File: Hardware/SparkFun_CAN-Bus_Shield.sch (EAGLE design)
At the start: 48 parts, among them Q1 16MHz, U1 USD-SOCKETNEW, U2 ARDUINO_R3_SHIELD, U3 JST_VERTICAL, U4 MCP2515, U5 MCP2551, U6 HEX_CONVERTER, X1 DB9 Plug

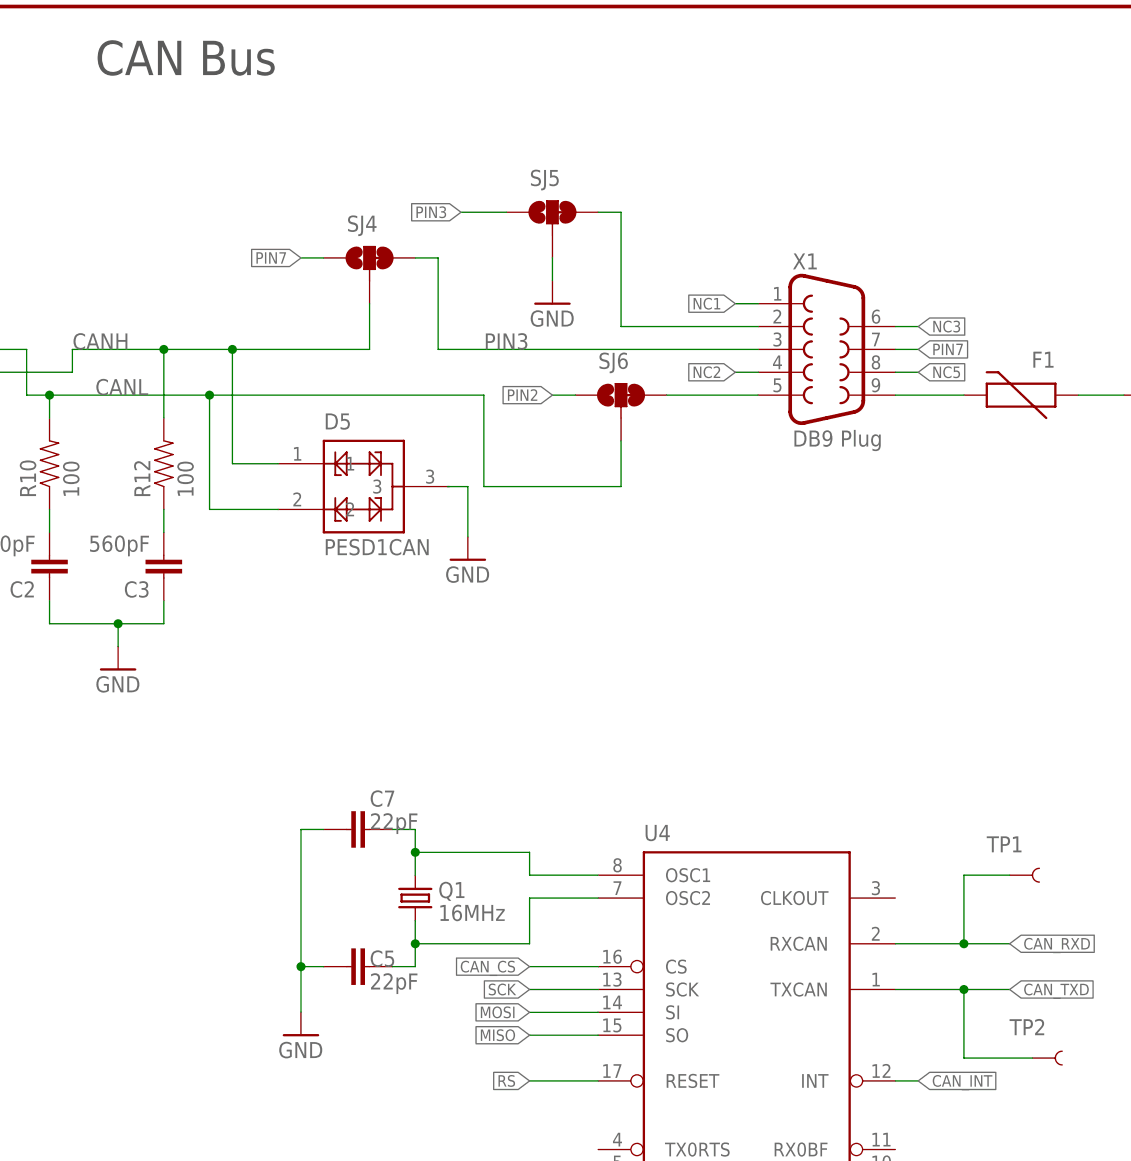
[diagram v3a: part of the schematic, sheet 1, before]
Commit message: Adding in feedback from Sukkin, and engineering review/QC checklist
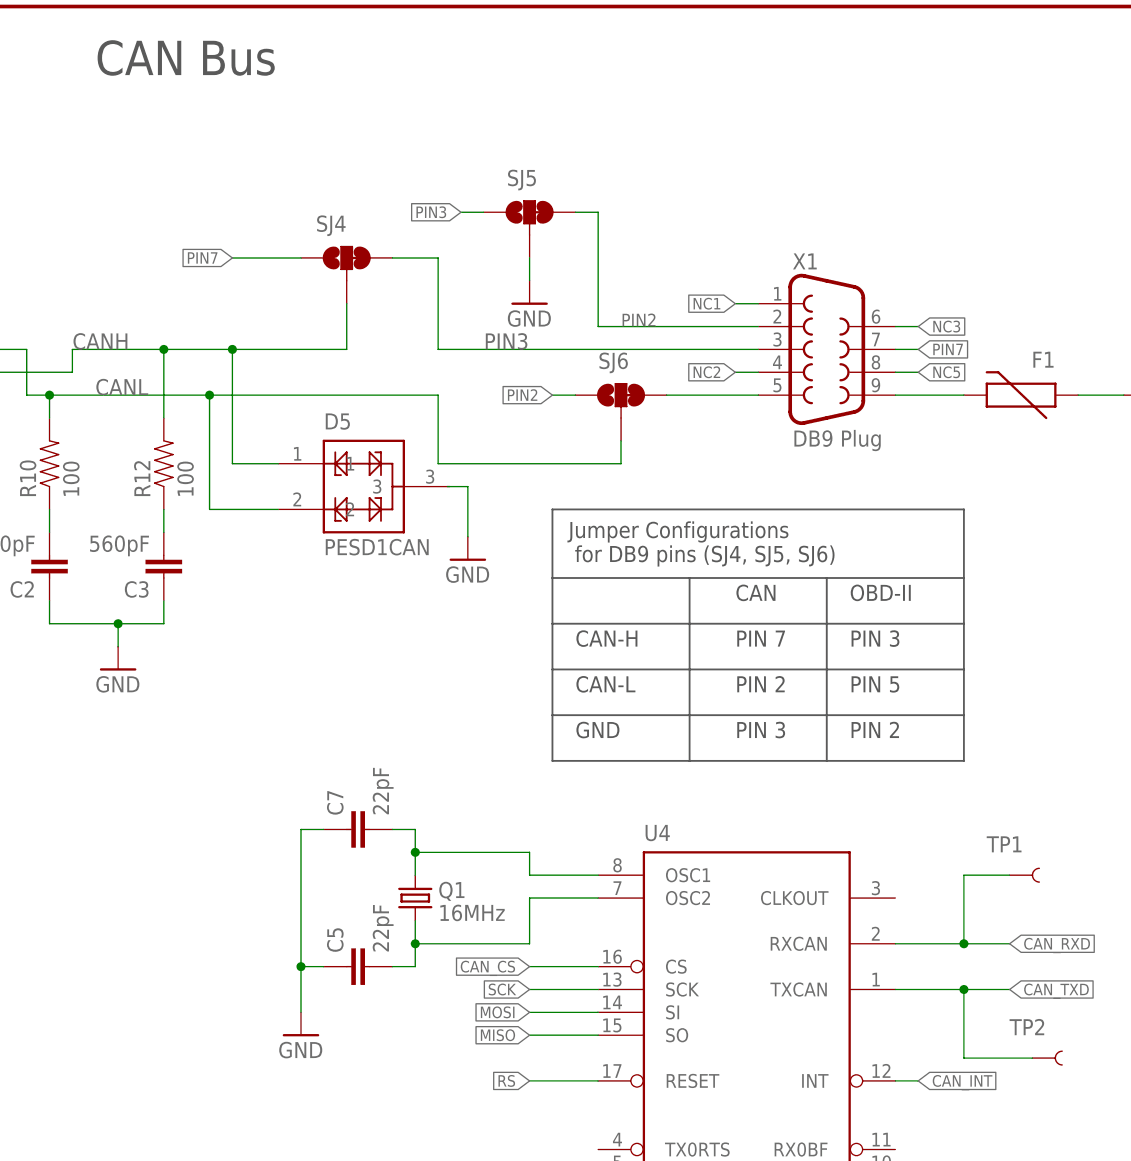
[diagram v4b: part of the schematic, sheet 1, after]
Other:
- note added: "CAN"
- note added: "CAN-H"
- note added: "CAN-L"
- note added: "GND"
- note added: "Jumper Configurations for DB9 pins (SJ4, SJ5, SJ6)"
- note added: "OBD-II"
- note added: "PIN 2"
- note added: "PIN 3"
- note added: "PIN 5"
- note added: "PIN 7"
- moved on the sheet: SJ4, SJ5
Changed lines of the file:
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@@
 <setting verticaltext="up"/>
 </settings>
-<grid distance="0.01" unitdist="inch" unit="inch" style="lines" multiple="1" display="no" altdistance="0.01" altunitdist="inch" altunit="inch"/>
+<grid distance="0.1" unitdist="inch" unit="inch" style="lines" multiple="1" display="no" altdistance="0.01" altunitdist="inch" altunit="inch"/>
 <layers>
 <layer number="1" name="Top" color="4" fill="1" visible="no" active="no"/>
@@
 <wire x1="91.44" y1="185.42" x2="93.98" y2="185.42" width="0.2032" layer="97" style="shortdash"/>
 <text x="99.06" y="177.8" size="3.81" layer="97">CAN Bus</text>
+<wire x1="149.86" y1="121.92" x2="165.1" y2="121.92" width="0.2032" layer="97"/>
+<wire x1="165.1" y1="121.92" x2="180.34" y2="121.92" width="0.2032" layer="97"/>
+<wire x1="180.34" y1="121.92" x2="195.58" y2="121.92" width="0.2032" layer="97"/>
+<wire x1="195.58" y1="121.92" x2="195.58" y2="116.84" width="0.2032" layer="97"/>
+<wire x1="195.58" y1="116.84" x2="195.58" y2="111.76" width="0.2032" layer="97"/>
+<wire x1="195.58" y1="111.76" x2="195.58" y2="106.68" width="0.2032" layer="97"/>
+<wire x1="195.58" y1="106.68" x2="195.58" y2="101.6" width="0.2032" layer="97"/>
+<wire x1="195.58" y1="101.6" x2="180.34" y2="101.6" width="0.2032" layer="97"/>
+<wire x1="180.34" y1="101.6" x2="165.1" y2="101.6" width="0.2032" layer="97"/>
+<wire x1="165.1" y1="101.6" x2="149.86" y2="101.6" width="0.2032" layer="97"/>
+<wire x1="149.86" y1="101.6" x2="149.86" y2="106.68" width="0.2032" layer="97"/>
+<wire x1="149.86" y1="106.68" x2="149.86" y2="111.76" width="0.2032" layer="97"/>
+<wire x1="149.86" y1="111.76" x2="149.86" y2="116.84" width="0.2032" layer="97"/>
+<wire x1="149.86" y1="116.84" x2="149.86" y2="121.92" width="0.2032" layer="97"/>
+<wire x1="149.86" y1="116.84" x2="195.58" y2="116.84" width="0.2032" layer="97"/>
+<wire x1="149.86" y1="111.76" x2="195.58" y2="111.76" width="0.2032" layer="97"/>
+<wire x1="149.86" y1="106.68" x2="195.58" y2="106.68" width="0.2032" layer="97"/>
+<wire x1="165.1" y1="121.92" x2="165.1" y2="101.6" width="0.2032" layer="97"/>
+<wire x1="180.34" y1="121.92" x2="180.34" y2="101.6" width="0.2032" layer="97"/>
+<text x="170.18" y="119.38" size="1.778" layer="97">CAN</text>
+<text x="182.88" y="119.38" size="1.778" layer="97">OBD-II</text>
+<text x="152.4" y="114.3" size="1.778" layer="97">CAN-H</text>
+<text x="152.4" y="109.22" size="1.778" layer="97">CAN-L</text>
+<text x="152.4" y="104.14" size="1.778" layer="97">GND</text>
+<text x="182.88" y="109.22" size="1.778" layer="97">PIN 5</text>
+<text x="182.88" y="104.14" size="1.778" layer="97">PIN 2</text>
+<text x="182.88" y="114.3" size="1.778" layer="97">PIN 3</text>
+<text x="170.18" y="109.22" size="1.778" layer="97">PIN 2</text>
+<text x="170.18" y="104.14" size="1.778" layer="97">PIN 3</text>
+<text x="170.18" y="114.3" size="1.778" layer="97">PIN 7</text>
+<wire x1="149.86" y1="121.92" x2="149.86" y2="129.54" width="0.2032" layer="97"/>
+<wire x1="149.86" y1="129.54" x2="195.58" y2="129.54" width="0.2032" layer="97"/>
+<wire x1="195.58" y1="129.54" x2="195.58" y2="121.92" width="0.2032" layer="97"/>
+<text x="151.638" y="123.698" size="1.778" layer="97">Jumper Configurations
+ for DB9 pins (SJ4, SJ5, SJ6)</text>
 </plain>
 <instances>
@@
 <attribute name="VALUE" x="137.16" y="83.82" size="1.778" layer="96"/>
 </instance>
-<instance part="C5" gate="G$1" x="129.54" y="78.74" smashed="yes" rot="R90">
-<attribute name="NAME" x="129.54" y="78.74" size="1.778" layer="95"/>
-<attribute name="VALUE" x="129.54" y="76.2" size="1.778" layer="96"/>
-</instance>
-<instance part="C7" gate="G$1" x="129.54" y="93.98" smashed="yes" rot="R90">
-<attribute name="NAME" x="129.54" y="96.52" size="1.778" layer="95"/>
-<attribute name="VALUE" x="129.54" y="93.98" size="1.778" layer="96"/>
-</instance>
+<instance part="C5" gate="G$1" x="129.54" y="78.74" rot="R90"/>
+<instance part="C7" gate="G$1" x="129.54" y="93.98" rot="R90"/>
 <instance part="GND12" gate="1" x="121.92" y="71.12"/>
 <instance part="GND6" gate="1" x="35.56" y="58.42"/>
@@
 <instance part="JP4" gate="G$1" x="91.44" y="0"/>
 <instance part="X1" gate="G$1" x="180.34" y="147.32"/>
-<instance part="GND5" gate="1" x="149.86" y="152.4"/>
+<instance part="GND5" gate="1" x="147.32" y="152.4"/>
 <instance part="JP5" gate="G$1" x="76.2" y="76.2" rot="R180"/>
 <instance part="P+12" gate="G$1" x="68.58" y="88.9" smashed="yes">
@@
 <attribute name="NAME" x="200.66" y="71.12" size="1.778" layer="95"/>
 </instance>
-<instance part="SJ4" gate="G$1" x="129.54" y="157.48" smashed="yes" rot="R90">
-<attribute name="NAME" x="127" y="160.401" size="1.778" layer="95"/>
-</instance>
-<instance part="SJ5" gate="G$1" x="149.86" y="162.56" smashed="yes" rot="R90">
-<attribute name="NAME" x="147.32" y="165.481" size="1.778" layer="95"/>
+<instance part="SJ4" gate="G$1" x="127" y="157.48" smashed="yes" rot="R90">
+<attribute name="NAME" x="127" y="162.179" size="1.778" layer="95" rot="R180"/>
+</instance>
+<instance part="SJ5" gate="G$1" x="147.32" y="162.56" smashed="yes" rot="R90">
+<attribute name="NAME" x="144.78" y="165.481" size="1.778" layer="95"/>
 </instance>
 <instance part="SJ6" gate="G$1" x="157.48" y="142.24" smashed="yes" rot="R90">
@@
 <pinref part="SJ5" gate="G$1" pin="2"/>
 <pinref part="GND5" gate="1" pin="GND"/>
-<wire x1="149.86" y1="157.48" x2="149.86" y2="154.94" width="0.1524" layer="91"/>
+<wire x1="147.32" y1="157.48" x2="147.32" y2="154.94" width="0.1524" layer="91"/>
 </segment>
 <segment>
@@
 <pinref part="R12" gate="G$1" pin="2"/>
 <wire x1="106.68" y1="147.32" x2="114.3" y2="147.32" width="0.1524" layer="91"/>
-<wire x1="114.3" y1="147.32" x2="129.54" y2="147.32" width="0.1524" layer="91"/>
-<wire x1="129.54" y1="147.32" x2="129.54" y2="152.4" width="0.1524" layer="91"/>
+<wire x1="114.3" y1="147.32" x2="127" y2="147.32" width="0.1524" layer="91"/>
+<wire x1="127" y1="147.32" x2="127" y2="152.4" width="0.1524" layer="91"/>
 <junction x="106.68" y="147.32"/>
 <pinref part="SJ4" gate="G$1" pin="2"/>
@@
 <wire x1="93.98" y1="142.24" x2="111.76" y2="142.24" width="0.1524" layer="91"/>
 <junction x="93.98" y="142.24"/>
-<wire x1="111.76" y1="142.24" x2="142.24" y2="142.24" width="0.1524" layer="91"/>
-<wire x1="142.24" y1="142.24" x2="142.24" y2="132.08" width="0.1524" layer="91"/>
-<wire x1="142.24" y1="132.08" x2="157.48" y2="132.08" width="0.1524" layer="91"/>
+<wire x1="111.76" y1="142.24" x2="137.16" y2="142.24" width="0.1524" layer="91"/>
+<wire x1="137.16" y1="142.24" x2="137.16" y2="134.62" width="0.1524" layer="91"/>
+<wire x1="137.16" y1="134.62" x2="157.48" y2="134.62" width="0.1524" layer="91"/>
 <pinref part="SJ6" gate="G$1" pin="2"/>
-<wire x1="157.48" y1="132.08" x2="157.48" y2="137.16" width="0.1524" layer="91"/>
+<wire x1="157.48" y1="134.62" x2="157.48" y2="137.16" width="0.1524" layer="91"/>
 <wire x1="111.76" y1="142.24" x2="111.76" y2="129.54" width="0.1524" layer="91"/>
 <junction x="111.76" y="142.24"/>
@@
 <wire x1="172.72" y1="147.32" x2="137.16" y2="147.32" width="0.1524" layer="91"/>
 <wire x1="137.16" y1="147.32" x2="137.16" y2="157.48" width="0.1524" layer="91"/>
-<wire x1="137.16" y1="157.48" x2="134.62" y2="157.48" width="0.1524" layer="91"/>
+<wire x1="137.16" y1="157.48" x2="132.08" y2="157.48" width="0.1524" layer="91"/>
 <pinref part="X1" gate="G$1" pin="3"/>
 <label x="142.24" y="147.32" size="1.778" layer="95"/>
@@
 <segment>
 <pinref part="SJ5" gate="G$1" pin="1"/>
-<wire x1="144.78" y1="162.56" x2="139.7" y2="162.56" width="0.1524" layer="91"/>
+<wire x1="142.24" y1="162.56" x2="139.7" y2="162.56" width="0.1524" layer="91"/>
 <label x="139.7" y="162.56" size="1.27" layer="95" rot="R180" xref="yes"/>
 </segment>
@@
 <segment>
 <pinref part="SJ4" gate="G$1" pin="1"/>
-<wire x1="124.46" y1="157.48" x2="121.92" y2="157.48" width="0.1524" layer="91"/>
-<label x="121.92" y="157.48" size="1.27" layer="95" rot="R180" xref="yes"/>
+<wire x1="121.92" y1="157.48" x2="114.3" y2="157.48" width="0.1524" layer="91"/>
+<label x="114.3" y="157.48" size="1.27" layer="95" rot="R180" xref="yes"/>
 </segment>
 </net>
@@
 <segment>
 <pinref part="X1" gate="G$1" pin="2"/>
-<wire x1="172.72" y1="149.86" x2="157.48" y2="149.86" width="0.1524" layer="91"/>
-<wire x1="157.48" y1="149.86" x2="157.48" y2="162.56" width="0.1524" layer="91"/>
-<wire x1="157.48" y1="162.56" x2="154.94" y2="162.56" width="0.1524" layer="91"/>
+<wire x1="172.72" y1="149.86" x2="154.94" y2="149.86" width="0.1524" layer="91"/>
+<wire x1="154.94" y1="149.86" x2="154.94" y2="162.56" width="0.1524" layer="91"/>
+<wire x1="154.94" y1="162.56" x2="152.4" y2="162.56" width="0.1524" layer="91"/>
 <pinref part="SJ5" gate="G$1" pin="3"/>
-</segment>
-<segment>
+<label x="157.48" y="149.86" size="1.4224" layer="95"/>
+</segment>
+<segment>

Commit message: Pushing QC checklist changes
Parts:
- TP1, TP2: value TEST-POINTTP_15TH_THRU -> TEST-POINT3X5; device SparkFun-Passives:TEST-POINTTP_15TH_THRU -> SparkFun-Passives:TEST-POINT3X5
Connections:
- net VCC renamed 5V
- net GND: now also D5.3, U1.CD1, U1.CD2; no longer U1.SHIELD@2, U1.SHIELD@4
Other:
- note added: "Revision by: Toni Klopfenstein"
- note added: "Switch jumpers to select between OBD-II or CAN pinout on DB9 connector. See table for configurations."
- moved on the sheet: C1, JP5, R13, U4P

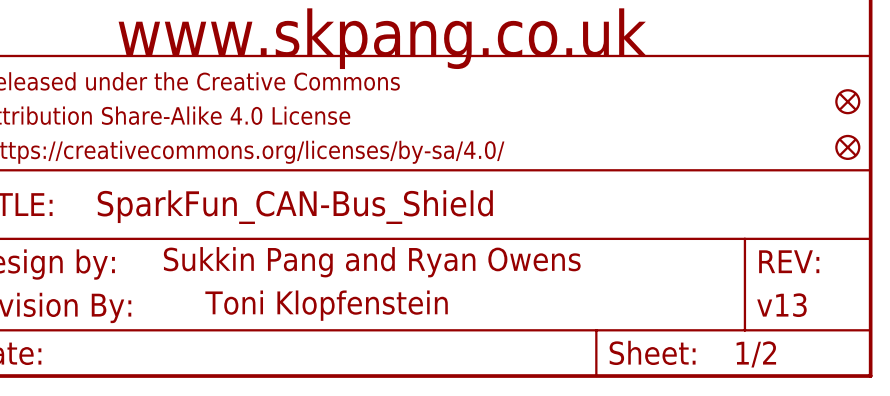
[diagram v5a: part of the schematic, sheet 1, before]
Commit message: Added production directory, updating shield units to pass QC check
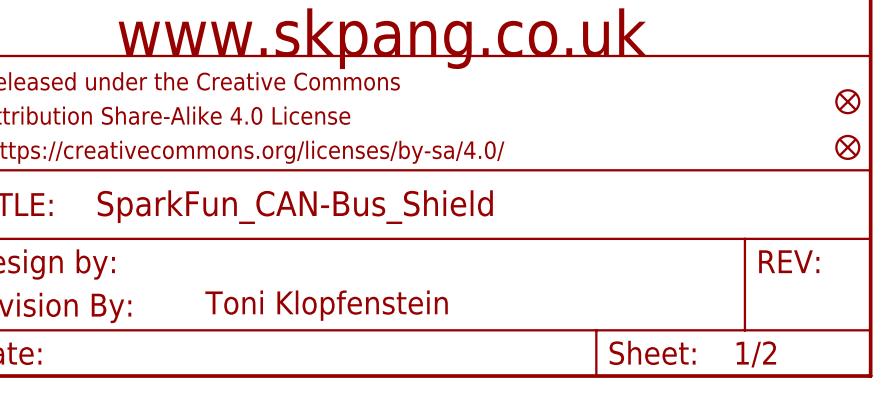
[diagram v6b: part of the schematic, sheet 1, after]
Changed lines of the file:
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@@
 <layer number="56" name="wert" color="7" fill="1" visible="no" active="no"/>
 <layer number="57" name="tCAD" color="7" fill="1" visible="no" active="no"/>
+<layer number="59" name="tCarbon" color="7" fill="1" visible="no" active="no"/>
+<layer number="60" name="bCarbon" color="7" fill="1" visible="no" active="no"/>
 <layer number="90" name="Modules" color="5" fill="1" visible="yes" active="yes"/>
 <layer number="91" name="Nets" color="2" fill="1" visible="yes" active="yes"/>
@@
 <layer number="113" name="IDFDebug" color="4" fill="1" visible="no" active="yes"/>
 <layer number="116" name="Patch_BOT" color="9" fill="4" visible="yes" active="yes"/>
+<layer number="118" name="Rect_Pads" color="7" fill="1" visible="yes" active="yes"/>
 <layer number="121" name="_tsilk" color="7" fill="1" visible="yes" active="yes"/>
 <layer number="122" name="_bsilk" color="7" fill="1" visible="yes" active="yes"/>
@@
 <layer number="127" name="_tValues" color="7" fill="1" visible="no" active="yes"/>
 <layer number="128" name="_bValues" color="7" fill="1" visible="no" active="yes"/>
+<layer number="129" name="Mask" color="7" fill="1" visible="yes" active="yes"/>
 <layer number="131" name="tAdjust" color="7" fill="1" visible="no" active="yes"/>
 <layer number="132" name="bAdjust" color="7" fill="1" visible="no" active="yes"/>
@@
 <layer number="223" name="223bmp" color="24" fill="1" visible="no" active="no"/>
 <layer number="224" name="224bmp" color="25" fill="1" visible="no" active="no"/>
+<layer number="225" name="225bmp" color="7" fill="1" visible="yes" active="yes"/>
+<layer number="226" name="226bmp" color="7" fill="1" visible="yes" active="yes"/>
+<layer number="227" name="227bmp" color="7" fill="1" visible="yes" active="yes"/>
+<layer number="228" name="228bmp" color="7" fill="1" visible="yes" active="yes"/>
+<layer number="229" name="229bmp" color="7" fill="1" visible="yes" active="yes"/>
+<layer number="230" name="230bmp" color="7" fill="1" visible="yes" active="yes"/>
+<layer number="231" name="231bmp" color="7" fill="1" visible="yes" active="yes"/>
 <layer number="248" name="Housing" color="7" fill="1" visible="no" active="yes"/>
 <layer number="249" name="Edge" color="7" fill="1" visible="no" active="yes"/>
@@
 <layer number="255" name="routoute" color="7" fill="1" visible="yes" active="yes"/>
 </layers>
-<schematic xreflabel="%F%N" xrefpart="/%S.%C%R">
+<schematic xreflabel="%F%N/%S" xrefpart="/%S">
 <attributes>
 </attributes>
